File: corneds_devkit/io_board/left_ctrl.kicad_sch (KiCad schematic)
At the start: 1 part

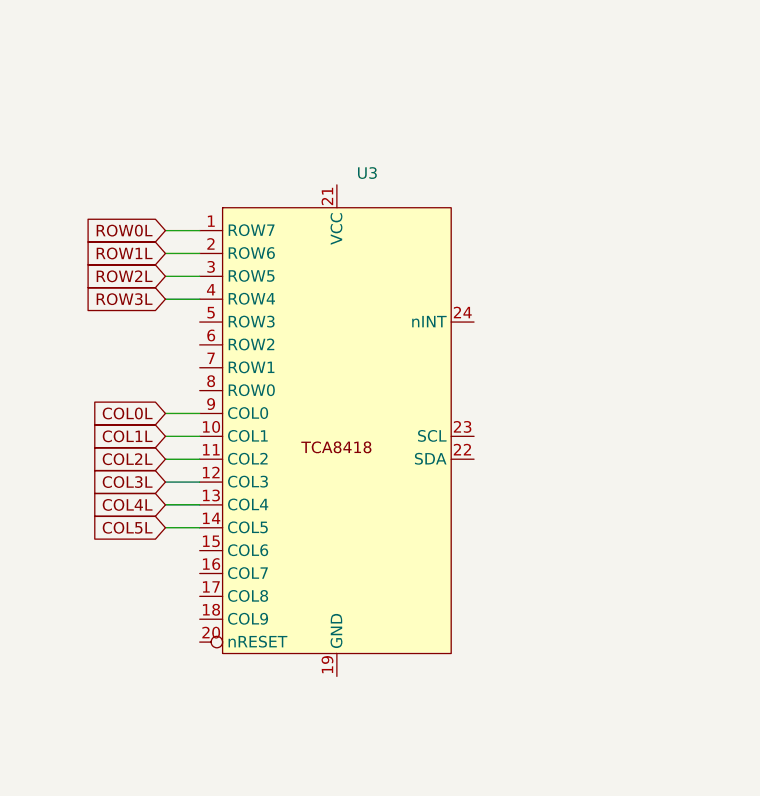
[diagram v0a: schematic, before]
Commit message: added switch footprint, io sch, and keypad IC footprint. Need to find new LEDs and make joystick footprint
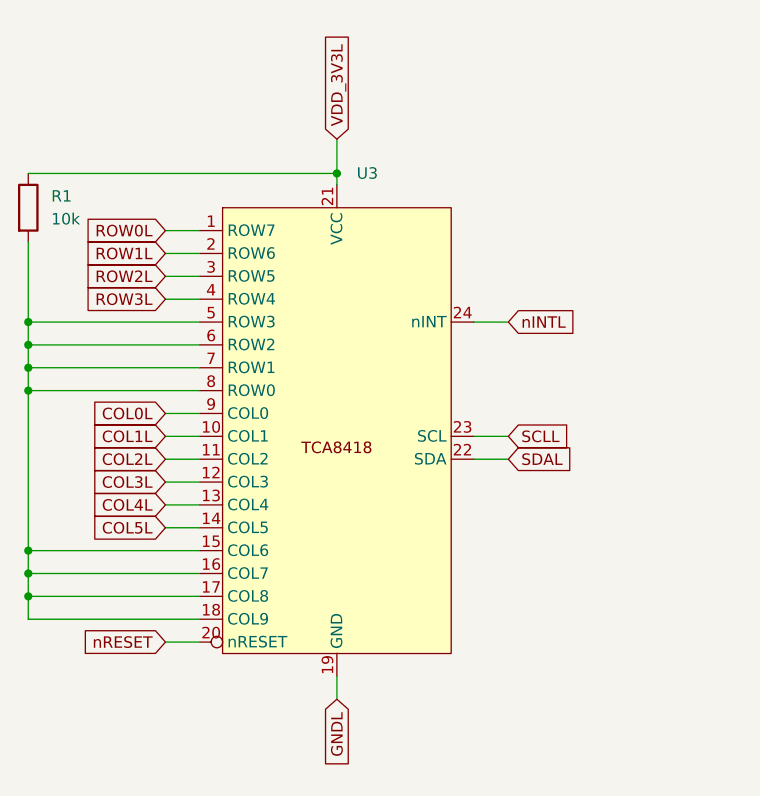
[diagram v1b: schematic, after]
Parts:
- added R1: 10k, Resistor_SMD:R_0402_1005Metric, symbol Device:R
- U3: footprint (none) -> Package_DFN_QFN:WQFN-24-1EP_4x4mm_P0.5mm_EP2.45x2.45mm
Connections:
- net at U3.15 (COL6): now also U3.16 (COL7), U3.17 (COL8), U3.18 (COL9), U3.5 (ROW3), U3.6 (ROW2), U3.7 (ROW1), U3.8 (ROW0), R1.2
- net GNDL: now reaches U3.19 (GND)
- net nRESET: now reaches U3.20 (nRESET)
- net VDD_3V3L: now reaches U3.21 (VCC)
- net VDD_3V3L: now also R1.1
- net SDAL: now reaches U3.22 (SDA)
- net SCLL: now reaches U3.23 (SCL)
- net nINTL: now reaches U3.24 (nINT)

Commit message: finished routing power board and started on control board schematic but realized I need seperate reset lines
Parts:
- added R12: 10k, Resistor_SMD:R_0402_1005Metric, symbol Device:R
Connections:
- net GNDL: now also R12.2
- net nINTL: now also R12.1
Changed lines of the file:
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@@
+	)
+	(junction
+		(at 165.1 69.85)
+		(diameter 0)
+		(color 0 0 0 0)
+	)
+	(junction
+		(at 135.89 110.49)
+		(diameter 0)
+		(color 0 0 0 0)
 	)
 	(junction
@@
 	(wire
 		(pts
+			(xy 165.1 110.49) (xy 135.89 110.49)
+		)
+		(stroke
+			(width 0)
+			(type default)
+		)
+	)
+	(wire
+		(pts
 			(xy 120.65 74.93) (xy 101.6 74.93)
 		)
@@
 	(wire
 		(pts
+			(xy 135.89 110.49) (xy 135.89 111.76)
+		)
+		(stroke
+			(width 0)
+			(type default)
+		)
+	)
+	(wire
+		(pts
+			(xy 165.1 77.47) (xy 165.1 110.49)
+		)
+		(stroke
+			(width 0)
+			(type default)
+		)
+	)
+	(wire
+		(pts
 			(xy 101.6 69.85) (xy 101.6 60.96)
 		)
@@
 	(wire
 		(pts
-			(xy 135.89 109.22) (xy 135.89 111.76)
-		)
-		(stroke
-			(width 0)
-			(type default)
-		)
-	)
-	(wire
-		(pts
-			(xy 151.13 69.85) (xy 154.94 69.85)
+			(xy 165.1 69.85) (xy 171.45 69.85)
+		)
+		(stroke
+			(width 0)
+			(type default)
+		)
+	)
+	(wire
+		(pts
+			(xy 135.89 109.22) (xy 135.89 110.49)
+		)
+		(stroke
+			(width 0)
+			(type default)
+		)
+	)
+	(wire
+		(pts
+			(xy 151.13 69.85) (xy 165.1 69.85)
 		)
 		(stroke
@@
 	(global_label "nINTL"
 		(shape input)
-		(at 154.94 69.85 0)
+		(at 171.45 69.85 0)
 		(fields_autoplaced yes)
 		(effects
@@
 		)
 		(property "Intersheetrefs" "${INTERSHEET_REFS}"
-			(at 163.0052 69.85 0)
+			(at 179.5152 69.85 0)
 			(effects
 				(font
@@
 					(unit 1)
 				)
+			)
+		)
+	)
+	(symbol
+		(lib_id "Device:R")
+		(at 165.1 73.66 0)
+		(unit 1)
+		(exclude_from_sim no)
+		(in_bom yes)
+		(on_board yes)
+		(dnp no)
+		(fields_autoplaced yes)
+		(property "Reference" "R12"
+			(at 167.64 72.3899 0)
+			(effects
+				(font
+					(size 1.27 1.27)
+				)
+				(justify left)
+			)
+		)
+		(property "Value" "10k"
+			(at 167.64 74.9299 0)
+			(effects
+				(font
+					(size 1.27 1.27)
+				)
+				(justify left)
+			)
+		)
+		(property "Footprint" "Resistor_SMD:R_0402_1005Metric"
+			(at 163.322 73.66 90)
+			(effects
+				(font
+					(size 1.27 1.27)
+				)
+				(hide yes)
+			)
+		)
+		(property "Datasheet" "~"
+			(at 165.1 73.66 0)
+			(effects
+				(font
+					(size 1.27 1.27)
+				)
+				(hide yes)
+			)
+		)
+		(property "Description" "Resistor"
+			(at 165.1 73.66 0)
+			(effects
+				(font
+					(size 1.27 1.27)
+				)
+				(hide yes)
+			)
+		)
+		(pin "1"
+		)
+		(pin "2"
+		)
+		(instances
+			(project "io_board"
+				(path "/244b6d6b-132d-4d50-ae86-e41103b29008/aa24d198-d69c-43fd-9b48-feffdb79bb14"
+					(reference "R12")
+					(unit 1)
+				)
